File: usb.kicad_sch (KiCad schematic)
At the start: 80 parts, among them J1 USB_C_Receptacle_USB2.0, J2 USB_C_Receptacle_USB2.0, J3 USB_C_Receptacle_USB2.0, J4 USB_C_Receptacle_USB2.0, U1 MIMX8MM6DVTLZAA, U10 D5V0H1B2LP, U11 TPD4E02B04, U12 TPD4E02B04, U13 74LVC2G07, U14 D5V0H1B2LP, U15 CH343P, U16 TPD4E02B04, U17 INA231, U18 D5V0H1B2LP, U19 TS3USB221E, U20 TPD4E02B04, U4 74LVC2G04, U5 NX5P3363, U6 TUSB320LAI, U7 NX5P3363, U8 TUSB320LAI, U9 D5V0H1B2LP

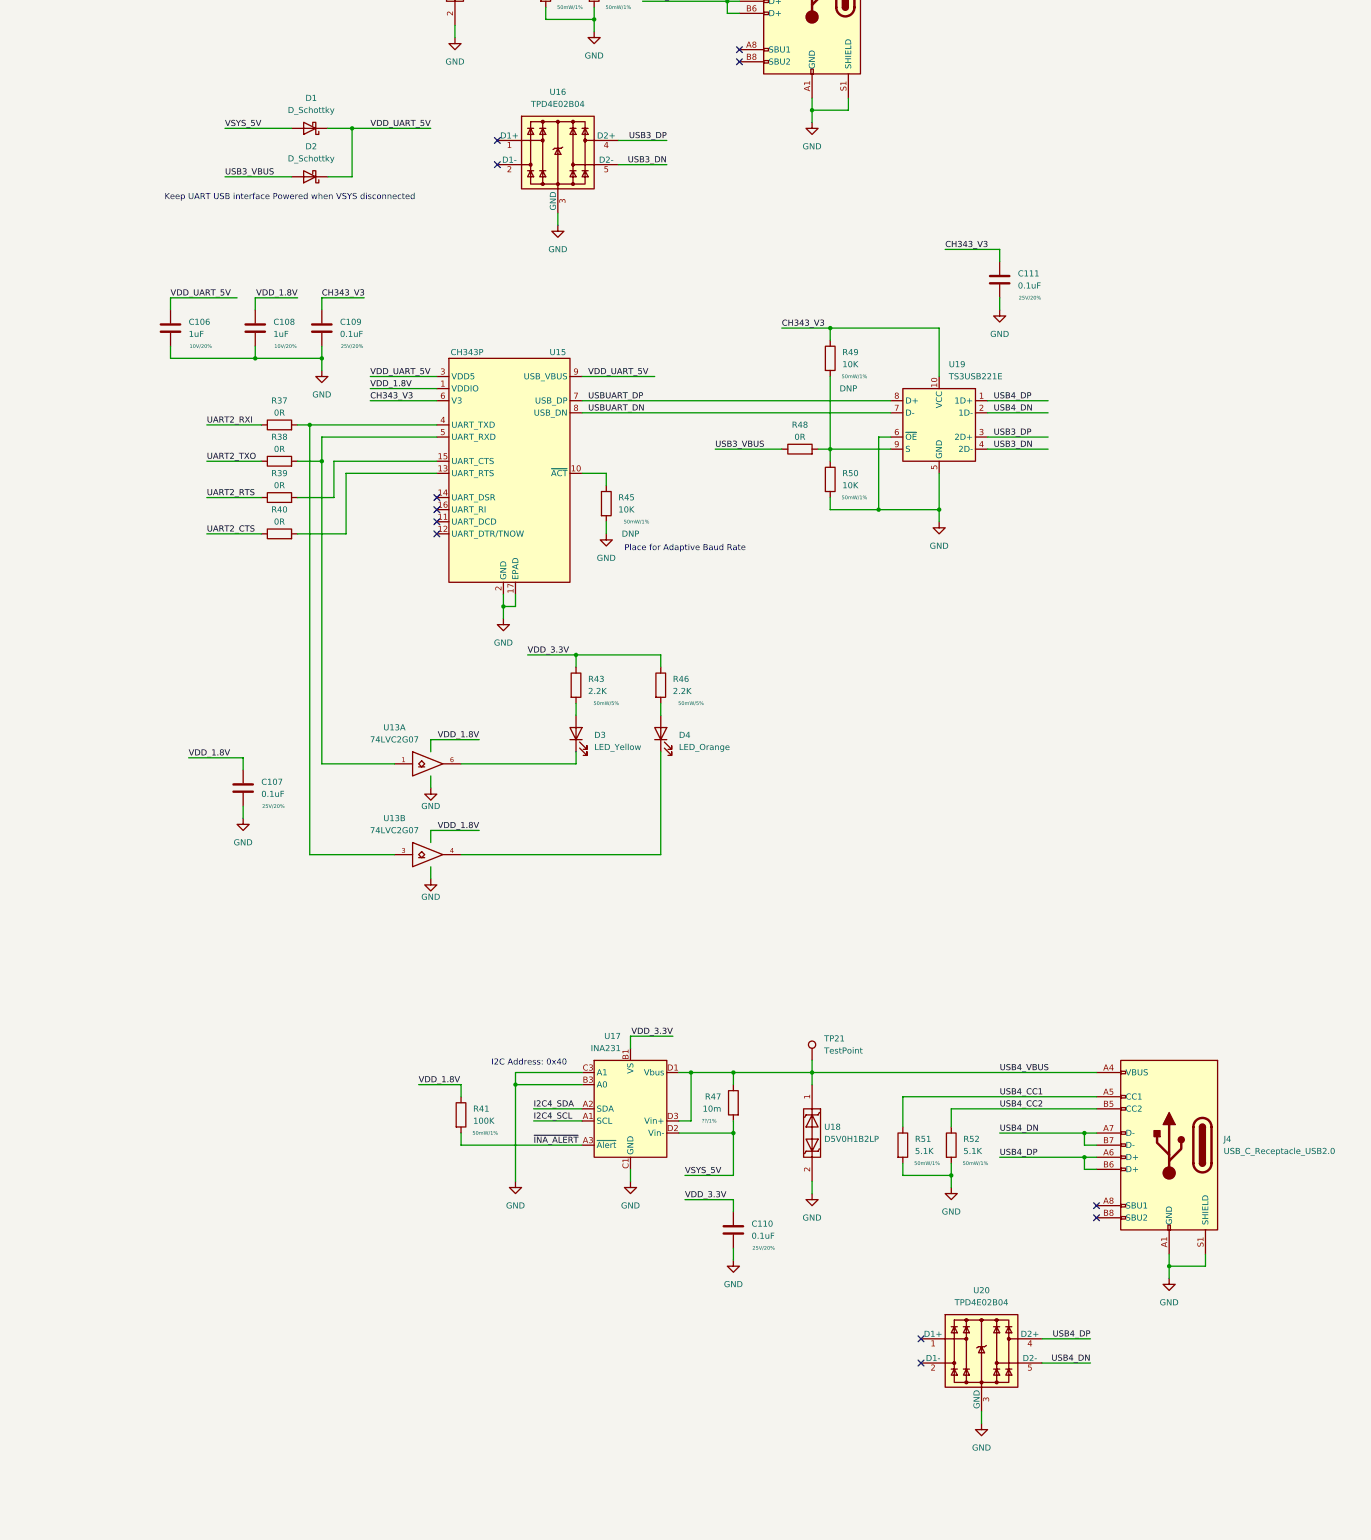
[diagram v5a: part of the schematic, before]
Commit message: change USB-UART conn, add new 0402 fp, more pcb work
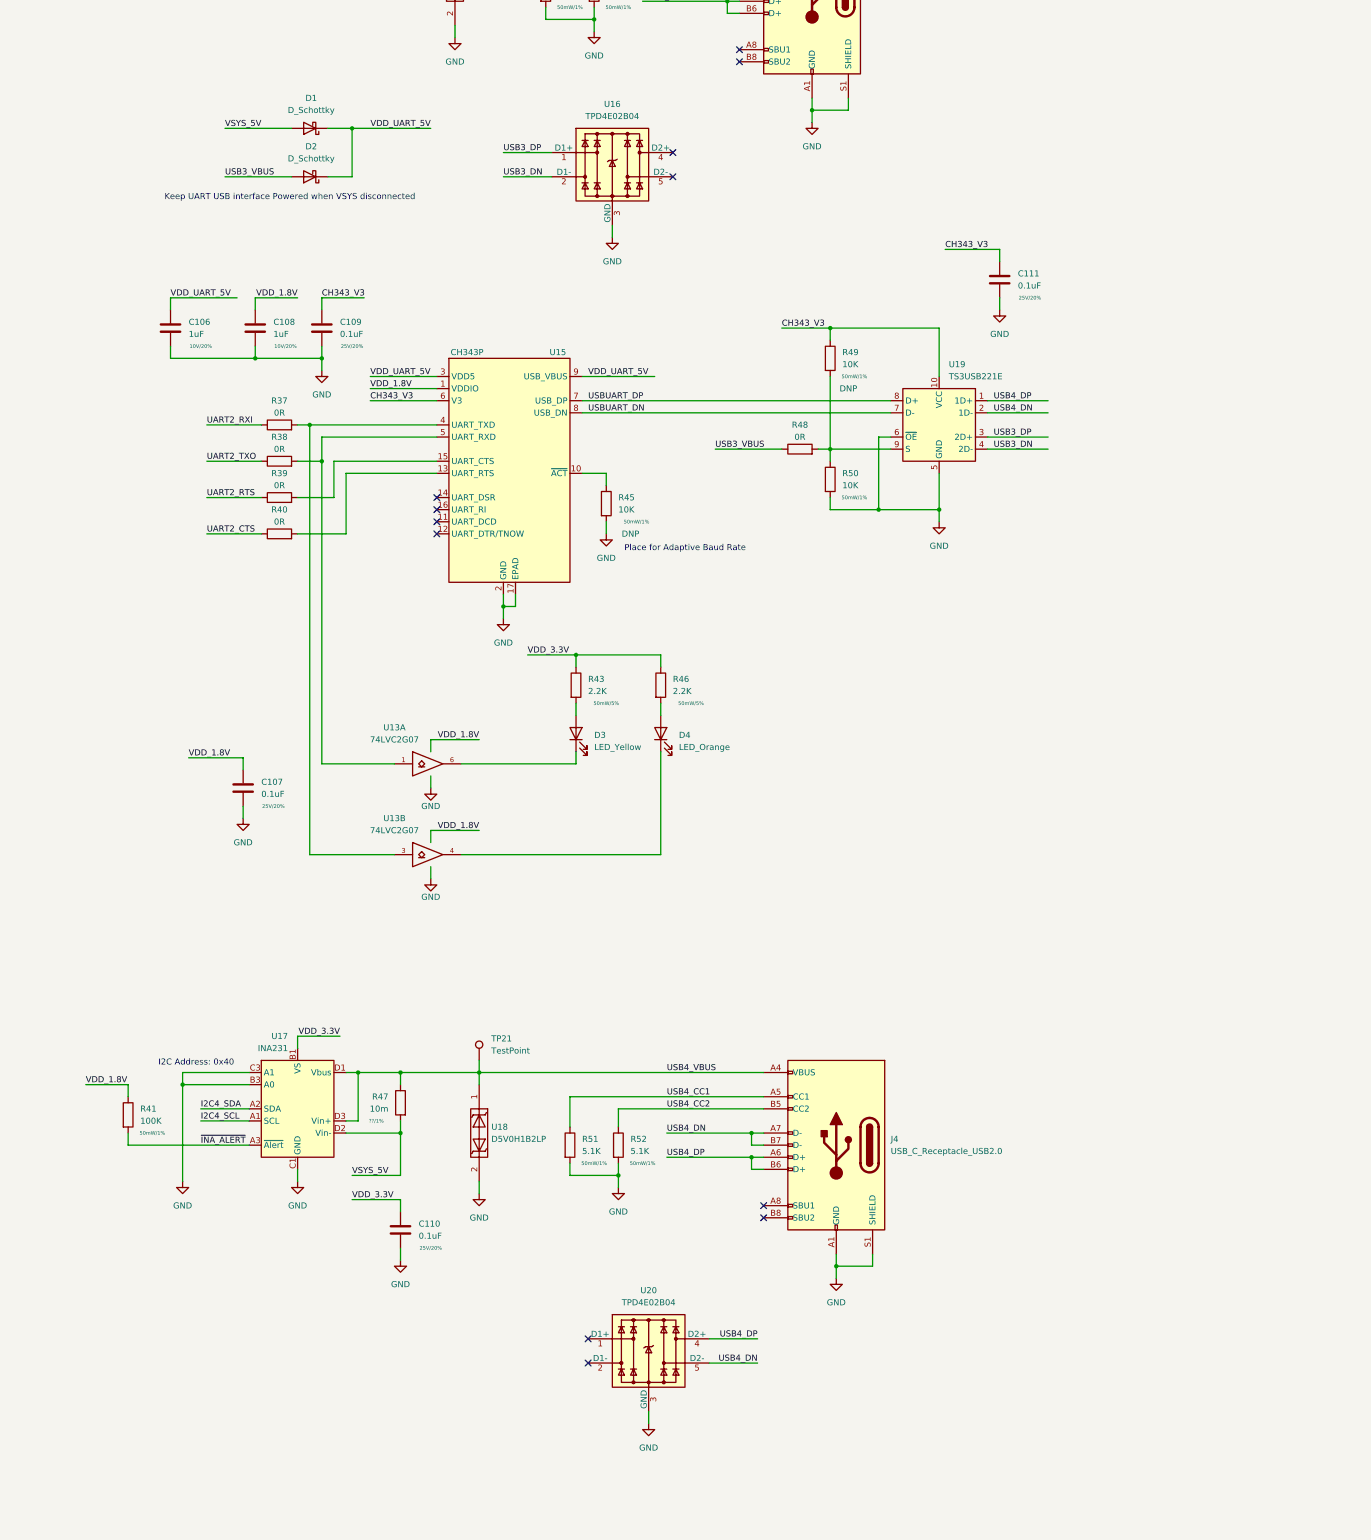
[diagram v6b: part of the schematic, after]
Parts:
- C100, C101, C106, C107, C108, C109, C110, C111, C95, C96, C97, C98, C99: footprint Capacitor_SMD:C_0402_1005Metric -> qsbc:C_0402_1005Metric
- J3: footprint qsbc:12402054M611A -> qsbc:KUSBX-SL-CS1N14-B
- R17, R18, R19, R20, R21, R22, R23, R24, R25, R26, R27, R28, R31, R32, R37, R38, R39, R40, R41, R42, R43, R44, R45, R46, R48, R49, R50, R51, R52: footprint Resistor_SMD:R_0402_1005Metric -> qsbc:R_0402_1005Metric
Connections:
- net USB3_DN: now also U16.2 (D1-), U16.9; no longer U16.5 (D2-), U16.6
- net USB3_DP: now also U16.1 (D1+), U16.10; no longer U16.4 (D2+), U16.7
- new net: U16.4 (D2+), U16.7
- new net: U16.5 (D2-), U16.6
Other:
- moved on the sheet: C110, J4, R41, R47, R51, R52, TP21, U16, U17, U18, U20

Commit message: place imx8mm/lpddr4 decoupling caps, lib cleanup
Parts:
- J1, J2, J4: footprint Connector_USB:USB_C_Receptacle_HRO_TYPE-C-31-M-12 -> qsbc:USB_C_Receptacle_USB4105-GF-A
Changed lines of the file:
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@@
       (effects (font (size 1.27 1.27)) (justify right))
     )
-    (property "Footprint" "Connector_USB:USB_C_Receptacle_HRO_TYPE-C-31-M-12" (id 2) (at 422.91 294.64 0)
+    (property "Footprint" "qsbc:USB_C_Receptacle_USB4105-GF-A" (id 2) (at 422.91 294.64 0)
       (effects (font (size 1.27 1.27)) hide)
     )
@@
       (effects (font (size 1.27 1.27)) (justify right))
     )
-    (property "Footprint" "Connector_USB:USB_C_Receptacle_HRO_TYPE-C-31-M-12" (id 2) (at 200.66 307.34 0)
+    (property "Footprint" "qsbc:USB_C_Receptacle_USB4105-GF-A" (id 2) (at 200.66 307.34 0)
       (effects (font (size 1.27 1.27)) hide)
     )
@@
       (effects (font (size 1.27 1.27)) (justify right))
     )
-    (property "Footprint" "Connector_USB:USB_C_Receptacle_HRO_TYPE-C-31-M-12" (id 2) (at 200.66 181.61 0)
-      (effects (font (size 1.27 1.27)) hide)
-    )
+    (property "Footprint" "qsbc:USB_C_Receptacle_USB4105-GF-A" (id 2) (at 200.66 181.61 0)
+      (effects (font (size 1.27 1.27)) hide)
+    )

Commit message: place / route SOC/DDR decoupling caps
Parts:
- R33, R34: footprint qsbc:R_0201_0603Metric -> qsbc:R_0402_1005Metric
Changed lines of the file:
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@@
       (effects (font (size 1.27 1.27)) (justify left))
     )
-    (property "Footprint" "qsbc:R_0201_0603Metric" (id 2) (at 183.642 78.74 90)
+    (property "Footprint" "qsbc:R_0402_1005Metric" (id 2) (at 183.642 78.74 90)
       (effects (font (size 1.27 1.27)) hide)
     )
@@
       (effects (font (size 1.27 1.27)) (justify left))
     )
-    (property "Footprint" "qsbc:R_0201_0603Metric" (id 2) (at 183.642 130.81 90)
-      (effects (font (size 1.27 1.27)) hide)
-    )
+    (property "Footprint" "qsbc:R_0402_1005Metric" (id 2) (at 183.642 130.81 90)
+      (effects (font (size 1.27 1.27)) hide)
+    )
